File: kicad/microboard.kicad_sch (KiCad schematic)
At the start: 12 parts, among them J2 to microboard, J3 to baseboard, U2 AH3712Q-P-B, U3 HT7550, U5 LM35-LP

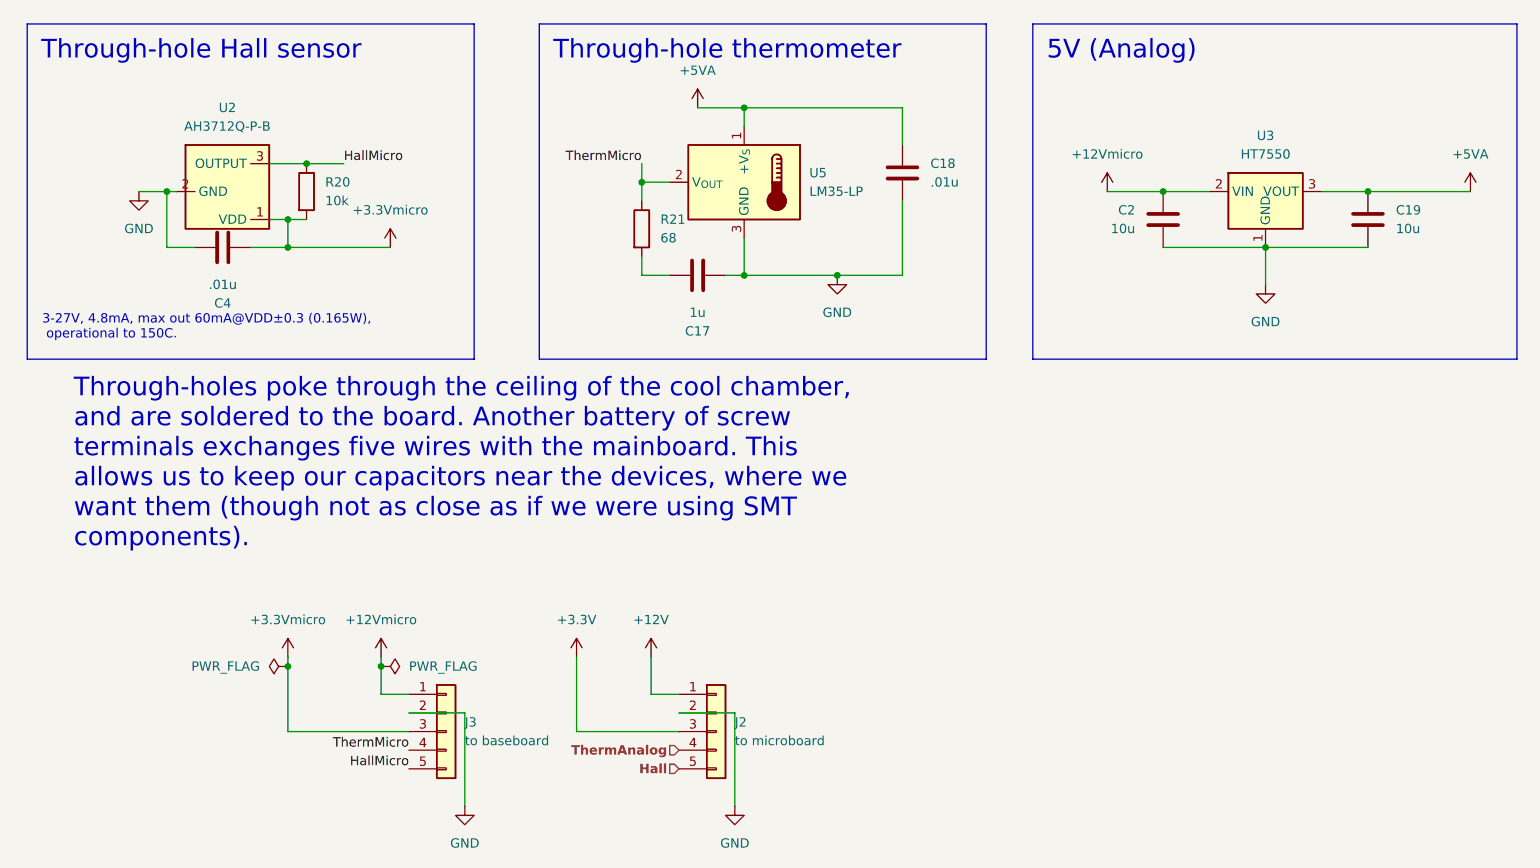
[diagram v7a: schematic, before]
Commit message: [miniboard] throughholes need [5, -5] separation #99
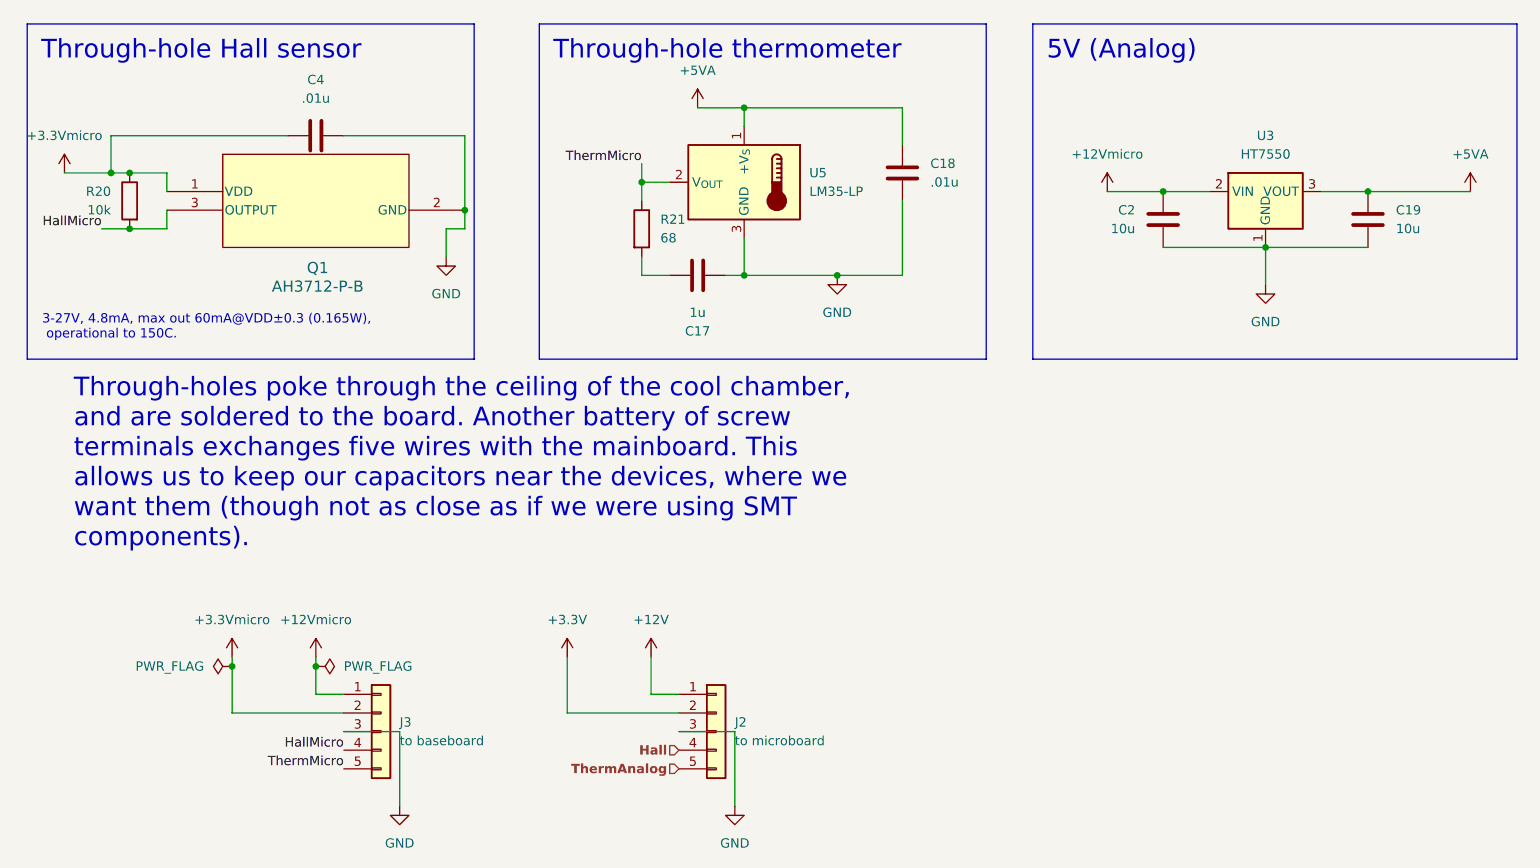
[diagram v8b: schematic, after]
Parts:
- removed U2: AH3712Q-P-B, dank:TRANS_AH3712-P-B_DIO, symbol dank:AH3712Q-P-B
- added Q1: AH3712-P-B, dank:TRANS_AH3712-P-B_DIO, symbol dank:AH3712-P-B
- C17, C18, C19, C2, C4: footprint Capacitor_SMD:C_1206_3216Metric_Pad1.33x1.80mm_HandSolder -> Capacitor_SMD:C_0805_2012Metric_Pad1.18x1.45mm_HandSolder
- R20, R21: footprint Resistor_SMD:R_1206_3216Metric_Pad1.30x1.75mm_HandSolder -> Resistor_SMD:R_0805_2012Metric_Pad1.20x1.40mm_HandSolder
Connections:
- net +3.3V: now also J2.2 (Pin_2); no longer J2.3 (Pin_3)
- net +3.3Vmicro: now also J3.2 (Pin_2), R20.1, Q1.1 (VDD); no longer J3.3 (Pin_3), R20.2
- net GND: now also J2.3 (Pin_3), J3.3 (Pin_3), Q1.2 (GND); no longer J2.2 (Pin_2), J3.2 (Pin_2)
- net Hall: now also J2.4 (Pin_4); no longer J2.5 (Pin_5)
- net HallMicro: now also J3.4 (Pin_4), R20.2, Q1.3 (OUTPUT); no longer J3.5 (Pin_5), R20.1
- net ThermAnalog: now also J2.5 (Pin_5); no longer J2.4 (Pin_4)
- net ThermMicro: now also J3.5 (Pin_5); no longer J3.4 (Pin_4)
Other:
- moved on the sheet: C4, J3, R20
